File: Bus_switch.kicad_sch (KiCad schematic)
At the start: 8 parts, among them J3 Conn_01x04_Pin, U1 SN74CB3Q3384APW

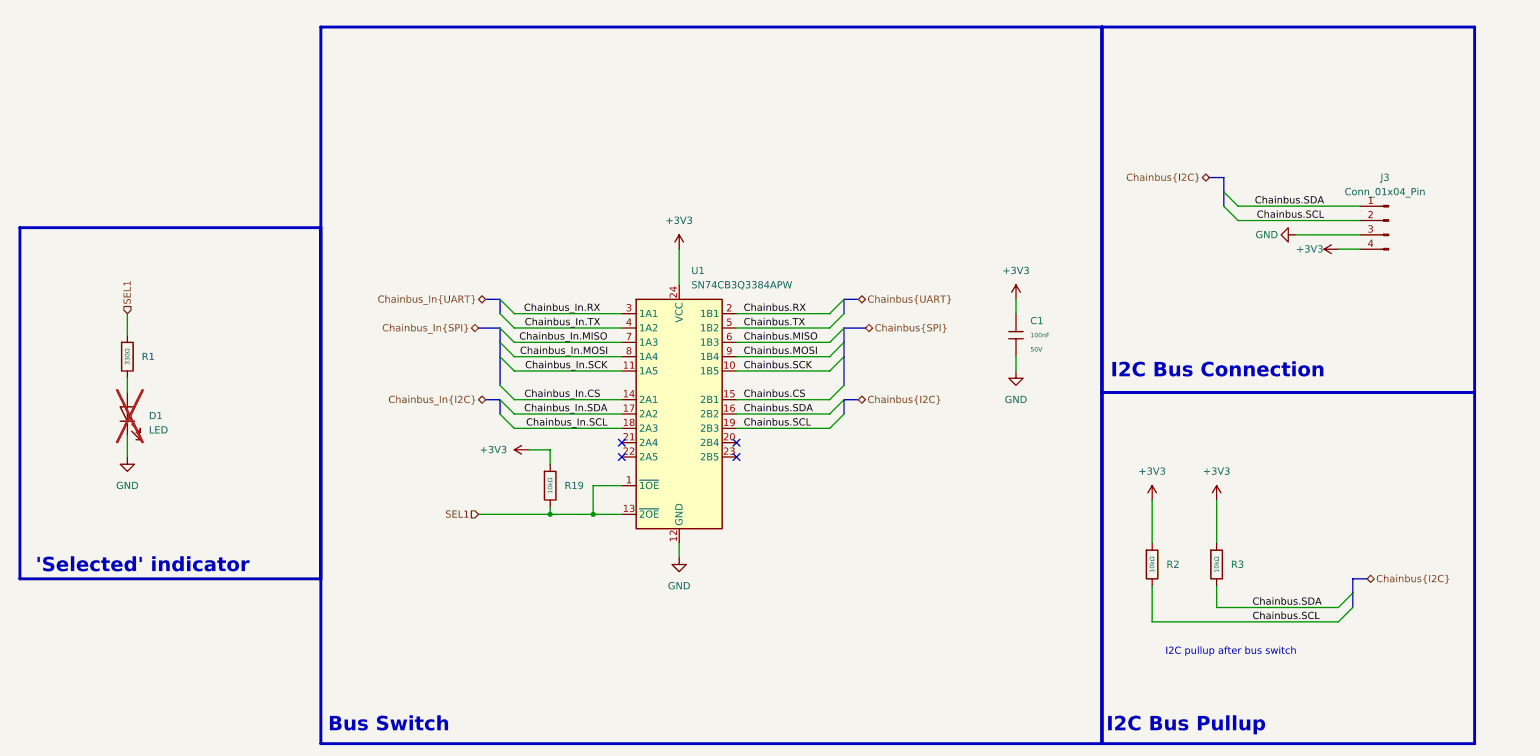
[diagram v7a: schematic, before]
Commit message: added pinout on silkscreen
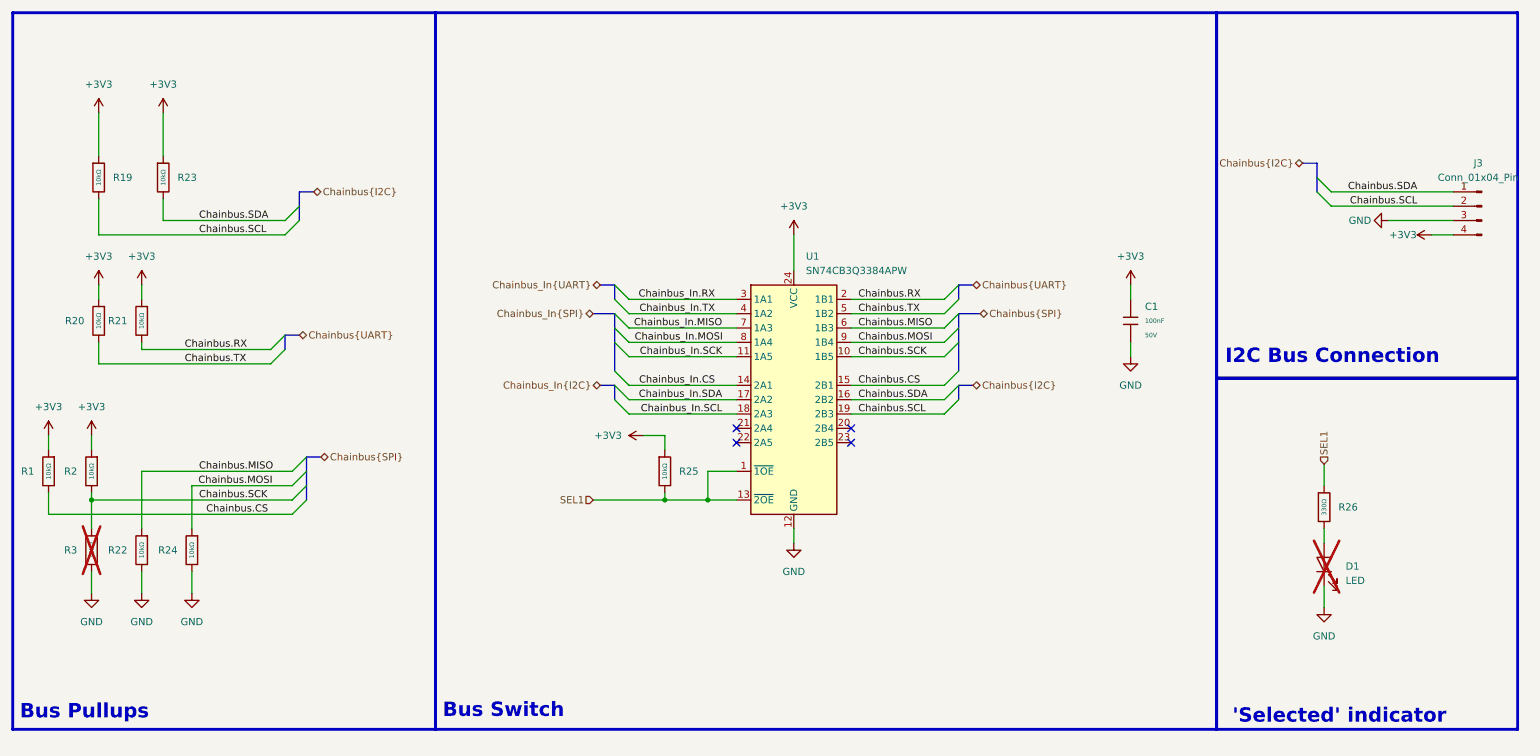
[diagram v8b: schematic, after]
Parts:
- added R1, R2, R20, R21, R22, R24, R3: 10kΩ, PCM_JLCPCB:R_0402, symbol PCM_JLCPCB-Resistors:0402,10kΩ
- renumbered R2 to R19, R3 to R23, R19 to R25, R1 to R26
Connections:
- net +3V3: now also R1.1, R2.1, R20.1, R21.1
- net Chainbus.CS: now also R1.2
- net Chainbus.MISO: now also R22.1
- net Chainbus.MOSI: now also R24.1
- net Chainbus.RX: now also R21.2
- net Chainbus.SCK: now also R2.2, R3.1
- net Chainbus.TX: now also R20.2
- net GND: now also R22.2, R24.2, R3.2
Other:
- note added: "Bus Pullups"
- note removed: "I2C Bus Pullup"
- note removed: "I2C pullup after bus switch"
- moved on the sheet: C1, D1, J3, R19, R23, R25, R26, U1
